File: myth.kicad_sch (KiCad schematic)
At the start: 225 parts, among them J1 Conn_01x08_Male, J2 Conn_01x08_Male, J4 Conn_01x08_Male, J5 Conn_01x08_Male, J6 Conn_01x08_Male, U1 74AHC02, U10 74HC595, U100 74AHC08, U101 74LS32, U102 74LS08, U103 74HC00, U104 74LS08, U105 74AHC02, U106 74LS08, U107 74LS08, U108 74LS08, U109 74LS573, U11 74HC165, U110 74LS573, U111 74HC157, U112 74HC157, U113 74HC157, U114 74AHC08, U115 4002, U116 4072, U117 74LS573, U118 74LS32, U119 74LS573, U12 74AHC08, U120 74LS573, U121 74AHC273, U122 74HC157, U123 74LS32, U124 74AHC04, U125 74LS573, U126 74LS573, U127 74AHC08, U128 74LS27, U129 74HC00, U13 74HC238, U130 74AHC08, U131 74LS573, U132 74HC74, U133 4072, U134 4072, U135 4078, U136 74AHC244, U137 74LS32, U138 74LS32, U139 74HC85, U14 74HC238, U140 74LS32, U141 74LS32, U142 74AHC04, U143 74AHC374, U144 74LS32, U145 4078, U146 74AHC08, U147 74LS573, U148 74LS573, U149 74LS573, U15 74HC238, U150 4070, U151 4070, U152 74AHC08, U153 4070, U154 4070, U155 4070, U156 4070, U157 4070, U158 74AHC08, U159 74AHC08, U16 74LS27, U160 74LS32, U161 74LS32, U162 74LS32, U163 74LS32, U164 74LS32, U165 74LS32, U166 74LS32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

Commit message: Clarify that only TRAP 0 sets BUSY as side-effect
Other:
- note added: "PHA0: Put page index (C or R) and byte offset (PC) of instruction on address bus PHA1: Latch opcode or IRQ Trap opcode into IB0-7, pre-decode instruction PHA2: Decode instruction, set up source byte on DB or other action PHA3: Latch results into target registers or other action CLOSE: Finish latching results, reset clock counter"
- note removed: "PHA0: Put page index (C) and byte offset (PC) of instruction on address bus PHA1: Latch opcode or IRQ Trap opcode into IB0-7, pre-decode instruction PHA2: Decode instruction, set up source byte on DB or other action PHA3: Latch results into target registers or other action CLOSE: Finish latching results, reset clock counter"
- moved on the sheet: J1, J2, J4, J5, J6, R1, RN1, RN2, U10, U100D, U101D, U102B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

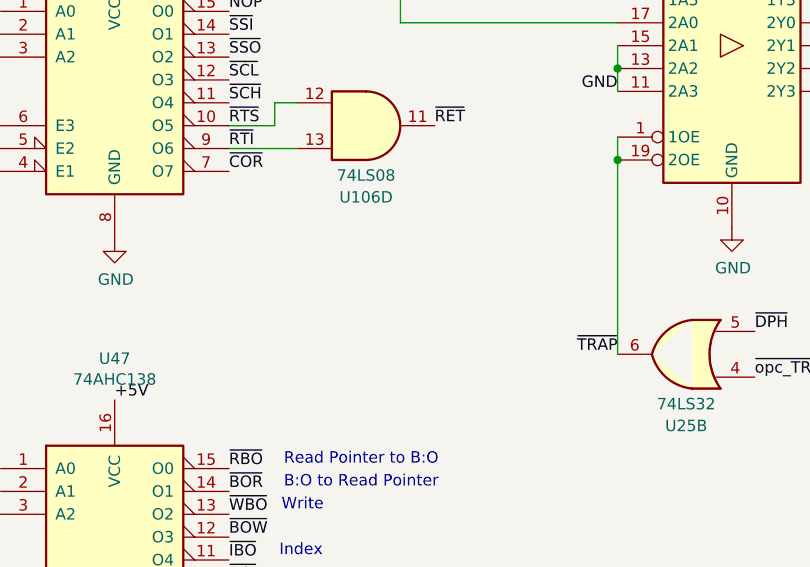
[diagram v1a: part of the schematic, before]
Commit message: Comment regarding RTI vs. EIN
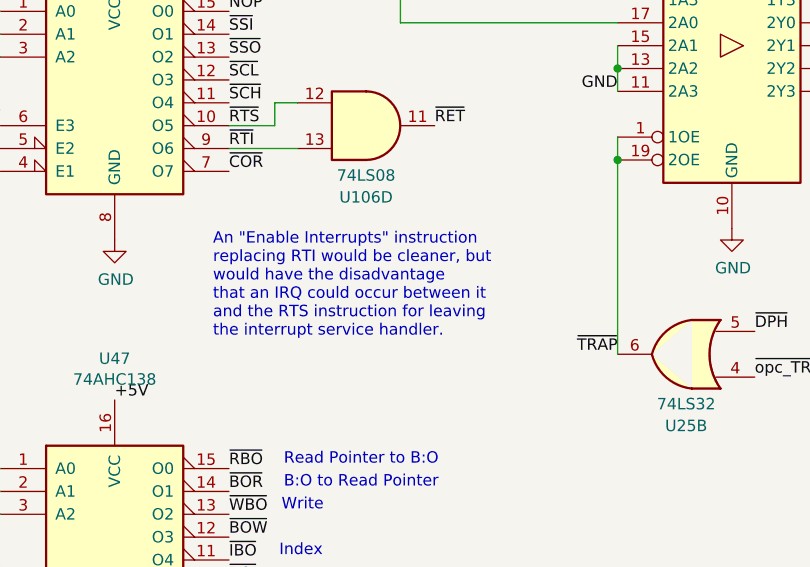
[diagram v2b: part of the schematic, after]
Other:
- note added: "An "Enable Interrupts" instruction replacing RTI would be cleaner, but would have the disadvantage that an IRQ could occur between it and the RTS instruction for leaving the interrupt service handler."
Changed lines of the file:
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@@
+		)
+	)
+	(text "An \"Enable Interrupts\" instruction\nreplacing RTI would be cleaner, but\nwould have the disadvantage\nthat an IRQ could occur between it\nand the RTS instruction for leaving\nthe interrupt service handler."
+		(exclude_from_sim no)
+		(at 289.052 557.022 0)
+		(effects
+			(font
+				(size 1.27 1.27)
+			)
+			(justify left bottom)
 		)
 	)

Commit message: Change mnemonics for BOP transfers
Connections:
- net BOI renamed SET_TP
- net BOR renamed SET_RP
- net BOS renamed SET_SP
- net BOW renamed SET_IP
- net IBO renamed GET_SP
- net LATCH_BOPTR renamed LATCH_POINTER
- net RBO renamed GET_IP
- net SBO renamed GET_TP
- net WBO renamed GET_RP
- net ~{BOI} renamed ~{SET_TP}
- net ~{BOR} renamed ~{SET_RP}
- net ~{BOS} renamed ~{SET_SP}
- net ~{BOW} renamed ~{SET_IP}
- net ~{IBO} renamed ~{GET_TP}
- net ~{RBO} renamed ~{GET_RP}
- net ~{SBO} renamed ~{GET_SP}
- net ~{WBO} renamed ~{GET_IP}
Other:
- note added: ""Index" Pointer, scratch"
- note added: ""Read" Pointer, scratch"
- note added: "GET = Pointer to B:O"
- note added: "GIP"
- note added: "GRP"
- note added: "GSP"
- note added: "GTP"
- note added: "SET = B:O to Pointer"
- note added: "SIP"
- note added: "SRP"
- note added: "SSP"
- note added: "STP"
- note added: "Stack Pointer (System Use)"
- note added: "Threading Pointer (System Use)"
- note removed: "B:O to Read Pointer"
- note removed: "Index"
- note removed: "Read Pointer to B:O"
- note removed: "Stack"
- note removed: "Write"
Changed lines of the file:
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@@
 	(title_block
 		(title "Sonne-8 Micro-Controller")
-		(date "2025-06-12")
+		(date "2025-06-13")
 		(rev "Myth")
 		(company "Contact: mim@ok-schalter.de")
@@
 		)
 	)
+	(text "\"Index\" Pointer, scratch"
+		(exclude_from_sim no)
+		(at 305.562 577.85 0)
+		(effects
+			(font
+				(size 1.27 1.27)
+			)
+			(justify left bottom)
+		)
+	)
 	(text "(Base)\nPage Index"
 		(exclude_from_sim no)
@@
 		)
 	)
+	(text "GIP"
+		(exclude_from_sim no)
+		(at 298.704 576.58 0)
+		(effects
+			(font
+				(size 1.27 1.27)
+			)
+			(justify left bottom)
+		)
+	)
 	(text "Outputs hardwired\noffset 80h"
 		(exclude_from_sim no)
@@
 		)
 	)
+	(text "GRP"
+		(exclude_from_sim no)
+		(at 298.704 571.5 0)
+		(effects
+			(font
+				(size 1.27 1.27)
+			)
+			(justify left bottom)
+		)
+	)
 	(text "Start, latch\ninstruction or\ninterrupt vector"
 		(exclude_from_sim no)
@@
 		)
 	)
+	(text "GSP"
+		(exclude_from_sim no)
+		(at 298.704 586.486 0)
+		(effects
+			(font
+				(size 1.27 1.27)
+			)
+			(justify left bottom)
+		)
+	)
 	(text "MxM"
 		(exclude_from_sim no)
@@
 		)
 	)
-	(text "B:O to Read Pointer"
+	(text "SET = B:O to Pointer"
 		(exclude_from_sim no)
-		(at 296.926 573.786 0)
+		(at 290.83 568.452 0)
 		(effects
 			(font
@@
 		)
 	)
+	(text "GTP"
+		(exclude_from_sim no)
+		(at 298.704 581.406 0)
+		(effects
+			(font
+				(size 1.27 1.27)
+			)
+			(justify left bottom)
+		)
+	)
 	(text "Copy old value of A into X"
 		(exclude_from_sim no)
@@
 		)
 	)
+	(text "SSP"
+		(exclude_from_sim no)
+		(at 298.704 589.026 0)
+		(effects
+			(font
+				(size 1.27 1.27)
+			)
+			(justify left bottom)
+		)
+	)
 	(text "                      -- Opcode Bits --\n                         MSB     LSB\n    all 0: OPC_SYS       00000   xxx    b0-2: Index of SYS Instruction\n     else: OPC_BOP       00001   xxx    b0-2: Index of BOP Instruction\n           OPC_ALU       0001   xxxx    b0-3: Index of ALU Instruction\n           OPC_TRAP      001   xxxxx    b0-4: DESTPAGE\n           OPC_GETPUT    01 xx x xxx    b0-2: OFFS, b3: GET/PUT, b4-5: REG\n           OPC_PAIR      1  xxx xxxx    b0-3: DST, b4-6: SRC"
 		(exclude_from_sim no)
@@
 		)
 	)
-	(text "Write"
-		(exclude_from_sim no)
-		(at 296.672 576.326 0)
-		(effects
-			(font
-				(size 1.27 1.27)
-			)
-			(justify left bottom)
-		)
-	)
 	(text "ALU EOR"
 		(exclude_from_sim no)
@@
 		)
 	)
-	(text "Stack"
+	(text "Stack Pointer (System Use)"
+		(exclude_from_sim no)
+		(at 305.816 586.994 0)
+		(effects
+			(font
+				(size 1.27 1.27)
+			)
+			(justify left bottom)
+		)
+	)
+	(text "SIP"
 		(exclude_from_sim no)
-		(at 296.672 586.486 0)
+		(at 298.704 579.12 0)
 		(effects
 			(font
@@
 		)
 	)
+	(text "STP"
+		(exclude_from_sim no)
+		(at 298.704 583.946 0)
+		(effects
+			(font
+				(size 1.27 1.27)
+			)
+			(justify left bottom)
+		)
+	)
 	(text "1"
 		(exclude_from_sim no)
@@
 		)
 	)
+	(text "\"Read\" Pointer, scratch"
+		(exclude_from_sim no)
+		(at 305.562 573.532 0)
+		(effects
+			(font
+				(size 1.27 1.27)
+			)
+			(justify left bottom)
+		)
+	)
 	(text "Jump if A negative"
 		(exclude_from_sim no)
@@
 		)
 	)
-	(text "Index"
+	(text "Threading Pointer (System Use)"
 		(exclude_from_sim no)
-		(at 296.418 581.406 0)
+		(at 305.562 582.168 0)
 		(effects
 			(font
@@
 		)
 	)
-	(text "Read Pointer to B:O"
+	(text "SRP"
+		(exclude_from_sim no)
+		(at 298.704 574.04 0)
+		(effects
+			(font
+				(size 1.27 1.27)
+			)
+			(justify left bottom)
+		)
+	)
+	(text "GET = Pointer to B:O"
 		(exclude_from_sim no)
-		(at 296.926 571.246 0)
+		(at 290.83 565.912 0)
 		(effects
 			(font
@@
 		)
 	)
-	(label "BOR"
+	(label "SET_RP"
 		(at 1120.14 681.99 180)
 		(effects
@@
 		)
 	)
+	(label "SET_SP"
+		(at 1120.14 511.81 180)
+		(effects
+			(font
+				(size 1.27 1.27)
+			)
+			(justify right bottom)
+		)
+	)
 	(label "C3"
 		(at 779.78 575.31 180)
@@
 		)
 	)
-	(label "BOS"
+	(label "SET_SP"
 		(at 1069.34 511.81 180)
 		(effects
@@
 		)
 	)
-	(label "~{SBO}"
+	(label "~{GET_SP}"
 		(at 1069.34 514.35 180)
 		(effects
@@
 		)
 	)
-	(label "BOI"
+	(label "SET_TP"
 		(at 1120.14 565.15 180)
 		(effects
@@
 		)
 	)
-	(label "~{RBO}"
+	(label "~{GET_RP}"
 		(at 290.83 571.5 0)
 		(effects
@@
 		)
 	)
-	(label "~{IBO}"
+	(label "~{GET_TP}"
 		(at 1120.14 567.69 180)
 		(effects
@@
 		)
 	)
-	(label "SBO"
+	(label "GET_TP"
 		(at 1112.52 439.42 180)
 		(effects
@@
 		)
 	)
-	(label "LATCH_BOPTR"
+	(label "LATCH_POINTER"
 		(at 896.62 414.02 180)
 		(effects
@@
 		)
 	)
-	(label "~{IBO}"
+	(label "~{GET_TP}"
 		(at 1069.34 567.69 180)
 		(effects
@@
 		)
 	)
-	(label "~{WBO}"
+	(label "~{GET_IP}"
 		(at 1120.14 631.19 180)
 		(effects
@@
 		)
 	)
-	(label "BOR"
+	(label "SET_RP"
 		(at 1066.8 681.99 180)
 		(effects
@@
 		)
 	)
-	(label "BOW"
+	(label "SET_IP"
 		(at 1066.8 628.65 180)
 		(effects
@@
 		)
 	)
-	(label "~{SBO}"
+	(label "~{GET_SP}"
 		(at 290.83 586.74 0)
 		(effects
@@
 		)
 	)
-	(label "BOI"
+	(label "SET_TP"
 		(at 1069.34 565.15 180)
 		(effects
@@
 		)
 	)
-	(label "RBO"
-		(at 1131.57 436.88 180)
+	(label "GET_RP"
+		(at 1131.57 434.34 180)
 		(effects
 			(font
@@
 		)
 	)
-	(label "~{RBO}"
+	(label "~{GET_RP}"
 		(at 1066.8 684.53 180)
 		(effects
@@
 		)
 	)
-	(label "~{BOR}"
+	(label "~{SET_RP}"
 		(at 290.83 574.04 0)
 		(effects
@@
 		)
 	)
-	(label "~{BOI}"
+	(label "~{SET_TP}"
 		(at 290.83 584.2 0)
 		(effects
@@
 		)
 	)
-	(label "BOW"
+	(label "SET_IP"
 		(at 1120.14 628.65 180)
 		(effects
@@
 		)
 	)
-	(label "~{IBO}"
+	(label "~{GET_TP}"
 		(at 290.83 581.66 0)
 		(effects
@@
 		)
 	)
-	(label "~{BOS}"
+	(label "~{SET_SP}"
 		(at 290.83 589.28 0)
 		(effects
@@
 		)
 	)
-	(label "BOS"
-		(at 1120.14 511.81 180)
-		(effects
-			(font
-				(size 1.27 1.27)
-			)
-			(justify right bottom)
-		)
-	)
 	(label "HI6"
 		(at 1145.54 504.19 0)
@@
 		)
 	)
-	(label "WBO"
-		(at 1131.57 434.34 180)
+	(label "GET_IP"
+		(at 1131.57 436.88 180)
 		(effects
 			(font
@@
 		)
 	)
-	(label "LATCH_BOPTR"
+	(label "LATCH_POINTER"
 		(at 737.87 595.63 180)
 		(effects
@@
 		)
 	)
-	(label "~{RBO}"
+	(label "~{GET_RP}"
 		(at 1120.14 684.53 180)
 		(effects
@@
 		)
 	)
-	(label "~{WBO}"
+	(label "~{GET_IP}"
 		(at 290.83 576.58 0)
 		(effects
@@
 		)
 	)
-	(label "~{BOW}"
+	(label "~{SET_IP}"
 		(at 290.83 579.12 0)
 		(effects
@@
 		)
 	)
-	(label "~{SBO}"
+	(label "~{GET_SP}"
 		(at 1120.14 514.35 180)
 		(effects
@@
 		)
 	)
-	(label "LATCH_BOPTR"
+	(label "LATCH_POINTER"
 		(at 1146.81 438.15 0)
 		(effects
@@
 		)
 	)
-	(label "IBO"
+	(label "GET_SP"
 		(at 1112.52 444.5 180)
 		(effects
@@
 		)
 	)
-	(label "~{WBO}"
+	(label "~{GET_IP}"
 		(at 1066.8 631.19 180)
 		(effects

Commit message: Rename R to G
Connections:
- net xR renamed xG
- net ~{xR} renamed ~{xG}
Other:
- note added: "(Guest-Page Index)"
- note added: "Adds 1 for 2's complement"
- note added: "G ("Guest") register provides code page-index for offsets >= 80h"
- note added: "Guest"
- note added: "OE except when xG"
- note added: "OE when xG"
- note added: "xG: sets page, branch to fixed offset 80h"
- note removed: "(Resident Page Index)"
- note removed: "OE except when xR"
- note removed: "OE when xR"
- note removed: "R ("Resident") register provides code page-index for offsets >= 80h"
- note removed: "Resident"
- note removed: "xR: sets page, branch to fixed offset 80h"
- moved on the sheet: U19, U22, U47

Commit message: Clean up schematics, rename BOP registers
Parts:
- removed U127: 74AHC08, Package_DIP:DIP-14_W7.62mm_Socket_LongPads, symbol 74xx:74LS08
- removed U137: 74LS32, Package_DIP:DIP-14_W7.62mm_Socket_LongPads, symbol 74xx:74LS32
- added U127: 74HC74, Package_DIP:DIP-14_W7.62mm_Socket_LongPads, symbol 74xx:74HC74
- added U219: 74LS32, Package_DIP:DIP-14_W7.62mm_Socket_LongPads, symbol 74xx:74LS32
- added U220: 74LS08, Package_DIP:DIP-14_W7.62mm_Socket_LongPads, symbol 74xx:74LS08
- added unit 4 of U42
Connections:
- net CLOSE: now also U42.12
- net GETO: now also U219.13
- net GND: now also U127.3 (C)
- net VCC: now also U127.2 (D); no longer U61.20 (VCC)
- net ~{GETO}: now also U220.5
- net ~{Ox}: now also U220.4
- net ~{xW}: now also U127.4 (~{S}); no longer U53.4 (DOWN)
- net at U134.5: now also U219.11
- net Px_pre: now reaches U15.7 (Y7)
- net Sx_pre: now reaches U15.9 (Y6)
- net xP_pre: now reaches U13.7 (Y7)
- net xS_pre: now reaches U13.9 (Y6)
- net at U123.11: now also U219.12
- net at U82.1 (1OE), U82.19 (2OE): now also U220.6
- net GET_IP renamed GSP
- net GET_RP renamed GCP
- net GET_SP renamed GTSP
- net GET_TP renamed GIP
- net O0_old renamed O_PC_0
- net O1_old renamed O_PC_1
- net O2_old renamed O_PC_2
- net O3_old renamed O_PC_3
- net O4_old renamed O_PC_4
- net O5_old renamed O_PC_5
- net O6_old renamed O_PC_6
- net O7_old renamed O_PC_7
- net SET_IP renamed SIP
- net SET_RP renamed STSP
- net SET_SP renamed SCP
- net SET_TP renamed SSP
- net ~{GET_IP} renamed ~{GIP}
- net ~{GIP}: now also U47.11 (O4); no longer U47.13 (O2)
- net ~{GET_RP} renamed ~{GTSP}
- net ~{GTSP}: now also U47.9 (O6); no longer U47.15 (O0)
- net ~{GET_SP} renamed ~{GCP}
- net ~{GCP}: now also U47.15 (O0); no longer U47.9 (O6)
- net ~{GET_TP} renamed ~{GSP}
- net ~{GSP}: now also U47.13 (O2); no longer U47.11 (O4)
- net ~{SET_IP} renamed ~{SSP}
- net ~{SET_RP} renamed ~{SCP}
- net ~{SET_SP} renamed ~{STSP}
- net ~{SET_TP} renamed ~{SIP}
- new net: U42.11, U53.4 (DOWN)
- new net: U127.5 (Q), U42.13
- new net ~{PHA0}: U127.1 (~{R})
- no-connect marks 44 -> 42
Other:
- note added: ""Copy" Pointer, scratch"
- note added: "ALU Instructions"
- note added: "B: - Saves page index of current instruction byte during call/trap/cor - Outputs return page index during RET - Is the (only) implied page index for memory read-write, with the corresponding byte offset stored in O (Offset) - Together with O forms a 16-bit address pointers subject to the xU instruction The B:O pointer can be loaded from/saved into the pointer registers"
- note added: "G"
- note added: "Index Pointer (ITC System Use)"
- note added: "O: - Saves offset of current instruction byte during call/trap/cor - Outputs return offset during RET - Is the (only) implied address offset for memory read-write, with the corresponding page index stored in B (Base) - Together with B forms 16-bit address pointers subject to the xU instruction. The B:O pointer can be loaded from/saved into the pointer registers"
- note added: "Outputs hardwired offset 80h for braching to guest routine (latched by PC, not O)"
- note added: "Parameter Stack Pointer (System Use)"
- note added: "Threading Stack Pointer (ITC System Use)"
- note removed: ""Index" Pointer, scratch"
- note removed: ""Read" Pointer, scratch"
- note removed: "B: - Saves page index of current instruction byte during call/trap/cor - Outputs return page index during RET - Is the (only) implied page index for memory read-write, with the corresponding byte offset stored in O (Offset) - Together with O forms a 16-bit address pointers subject to the xU instruction The B:O pointer can be loaded from/saved into the BO-Pointers P1-4"
- note removed: "GIP"
- note removed: "GRP"
- note removed: "GSP"
- note removed: "GTP"
- note removed: "O: - Saves offset of current instruction byte during call/trap/cor - Outputs return offset during RET - Is the (only) implied address offset for memory read-write, with the corresponding page index stored in B (Base) - Together with B forms 16-bit address pointers subject to the xU instruction. The B:O pointer can be loaded from/saved into the BO-Pointers P1-4"
- note removed: "Outputs hardwired offset 80h"
- note removed: "SIP"
- note removed: "SRP"
- note removed: "SSP"
- note removed: "STP"
- note removed: "Stack Pointer (System Use)"
- note removed: "Threading Pointer (System Use)"
- moved on the sheet: R1, RN1, RN2, U10, U100D, U101D, U102B, U102D, U103B, U104B, U104D, U105A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

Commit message: Rename BO pointers
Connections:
- net at U209.11, U80.11 (~{LOAD}), U83.11 (~{LOAD}): no longer U124.1
- net at U124.2: no longer U190.12
- net GCP renamed KBO
- net GIP renamed IBO
- net GSP renamed QBO
- net GTSP renamed TBO
- net SCP renamed BOK
- net SIP renamed BOI
- net SSP renamed BOQ
- net STSP renamed BOT
- net ~{GCP} renamed ~{KBO}
- net ~{GIP} renamed ~{IBO}
- net ~{GSP} renamed ~{QBO}
- net ~{GTSP} renamed ~{TBO}
- net ~{SCP} renamed ~{BOK}
- net ~{SIP} renamed ~{BOI}
- net ~{SSP} renamed ~{BOQ}
- net ~{STSP} renamed ~{BOT}
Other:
- note added: "(xU adds 8-bit signed to 16-bit B:O)"
- note added: "BO_ = B:O to Pointer"
- note added: "I"
- note added: "Interpreter Pointer (ITC System Use)"
- note added: "K"
- note added: "Key Pointer, scratch"
- note added: "Parameter Queue Pointer (System Use)"
- note added: "Q"
- note added: "T"
- note added: "Update"
- note added: "_BO: Pointer to B:O"
- note removed: ""Copy" Pointer, scratch"
- note removed: "GET = Pointer to B:O"
- note removed: "Index Pointer (ITC System Use)"
- note removed: "Parameter Stack Pointer (System Use)"
- note removed: "SET = B:O to Pointer"
- note removed: "Update (add 8-bit signed to 16-bit B:O)"
- moved on the sheet: U105A, U114D, U121, U124D, U127A, U12C, U130D, U135, U139, U142D, U143, U145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

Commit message: Fix displaced wire in schematics
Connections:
- net at U124.1: now also U209.11, U80.11 (~{LOAD}), U83.11 (~{LOAD})
- net at U124.2: now also U190.12
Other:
- note added: "Any of these disable the updating of X with pushed values or flags from A"
- note added: "Parameter Queue/Stack Pointer (System Use)"
- note removed: "Parameter Queue Pointer (System Use)"
- note removed: "These instructions prevent updating X"
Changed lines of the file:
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@@
 		)
 	)
-	(text "These instructions\nprevent updating X"
+	(text "Any of these disable\nthe updating of X with\npushed values or flags\nfrom A"
 		(exclude_from_sim no)
-		(at 1052.322 303.53 0)
+		(at 1015.238 314.706 0)
 		(effects
 			(font
@@
 	(text "ALU Instructions"
 		(exclude_from_sim no)
-		(at 529.336 196.596 0)
+		(at 525.78 192.024 0)
 		(effects
 			(font
@@
 		)
 	)
-	(text "Parameter Queue Pointer (System Use)"
+	(text "Parameter Queue/Stack Pointer (System Use)"
 		(exclude_from_sim no)
 		(at 290.83 585.978 0)
@@
 	)
 	(junction
+		(at 963.93 248.92)
+		(diameter 0)
+		(color 0 0 0 0)
+	)
+	(junction
 		(at 373.38 447.04)
 		(diameter 0)
@@
 	(wire
 		(pts
-			(xy 970.28 275.59) (xy 974.09 275.59)
+			(xy 963.93 276.86) (xy 967.74 276.86)
 		)
 		(stroke
@@
 	(wire
 		(pts
-			(xy 970.28 247.65) (xy 970.28 275.59)
+			(xy 963.93 248.92) (xy 963.93 276.86)
 		)
 		(stroke
@@
 	(symbol
 		(lib_id "74xx:74HC04")
-		(at 981.71 275.59 0)
+		(at 975.36 276.86 0)
 		(unit 1)
 		(exclude_from_sim no)
@@
 		(dnp no)
 		(property "Reference" "U124"
-			(at 981.71 267.5382 0)
+			(at 975.36 268.8082 0)
 			(effects
 				(font
@@
 		)
 		(property "Value" "74AHC04"
-			(at 981.71 269.8496 0)
+			(at 975.36 271.1196 0)
 			(effects
 				(font
@@
 		)
 		(property "Footprint" "Package_DIP:DIP-14_W7.62mm_Socket_LongPads"
-			(at 981.71 275.59 0)
+			(at 975.36 276.86 0)
 			(effects
 				(font
@@
 		)
 		(property "Datasheet" "https://assets.nexperia.com/documents/data-sheet/74HC_HCT04.pdf"
-			(at 981.71 275.59 0)
+			(at 975.36 276.86 0)
 			(effects
 				(font
@@
 		)
 		(property "Description" ""
-			(at 981.71 275.59 0)
+			(at 975.36 276.86 0)
 			(effects
 				(font
@@
 		(on_board yes)
 		(dnp no)
-		(fields_autoplaced yes)
 		(property "Reference" "U168"
-			(at 662.9317 49.53 0)
+			(at 670.052 51.308 0)
 			(effects
 				(font
@@
 		)
 		(property "Value" "74AHC08"
-			(at 662.9317 52.07 0)
+			(at 670.052 53.848 0)
 			(effects
 				(font
@@
 		(on_board yes)
 		(dnp no)
-		(fields_autoplaced yes)
 		(property "Reference" "U159"
-			(at 689.6017 49.53 0)
+			(at 697.484 51.308 0)
 			(effects
 				(font
@@
 		)
 		(property "Value" "74AHC08"
-			(at 689.6017 52.07 0)
+			(at 697.484 53.848 0)
 			(effects
 				(font
@@
 		(dnp no)
 		(property "Reference" "U180"
-			(at 232.41 65.2526 0)
+			(at 232.156 64.262 0)
 			(effects
 				(font
@@
 		)
 		(property "Value" "74HC157"
-			(at 232.41 67.564 0)
+			(at 232.156 66.5734 0)
 			(effects
 				(font
@@
 		(on_board yes)
 		(dnp no)
-		(fields_autoplaced yes)
 		(property "Reference" "U153"
-			(at 1020.7752 46.99 0)
+			(at 1027.7348 49.53 0)
 			(effects
 				(font
@@
 		)
 		(property "Value" "4070"
-			(at 1020.7752 49.53 0)
+			(at 1027.43 51.816 0)
 			(effects
 				(font
@@
 		(on_board yes)
 		(dnp no)
-		(fields_autoplaced yes)
 		(property "Reference" "U151"
-			(at 994.1052 46.99 0)
+			(at 999.744 49.276 0)
 			(effects
 				(font
@@
 		)
 		(property "Value" "4070"
-			(at 994.1052 49.53 0)
+			(at 999.744 51.816 0)
 			(effects
 				(font

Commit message: Document BOP registers, fix spec
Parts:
- removed U145: 4078, symbol 4xxx_IEEE:4078
- added U137: 4072, symbol 4xxx:4072
- added U221: 74LS32, Package_DIP:DIP-14_W7.62mm_Socket_LongPads, symbol 74xx:74LS32
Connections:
- net JUMP: now also U221.11
- net xG: now also U221.13
- net xJ: now also U137.3
- net at U7.8: now also U137.2
- net at U7.6: now also U137.4
- net at U38.6: now also U137.5
- new net: U137.1, U221.12
- no-connect marks 42 -> 41
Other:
- note added: "Branches to fixed offset 80h (on different page)"
- note added: "Key, scratch"
- note added: "Queue/Stack Pointer (System Use)"
- note removed: "Key Pointer, scratch"
- note removed: "Parameter Queue/Stack Pointer (System Use)"
- note removed: "xG: sets page, branch to fixed offset 80h"
- moved on the sheet: R1, RN1, RN2, U10, U101D, U102D, U104D, U105A, U107D, U108B, U108D, U11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
